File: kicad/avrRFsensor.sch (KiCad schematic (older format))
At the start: 26 parts, among them P1 CONN_1, P2 CONN_1, P3 CONN_1, P4 CONN_1, U1 ATMEGA168PA-A, U2 RFM69, X1 18MHz HC49USSMD

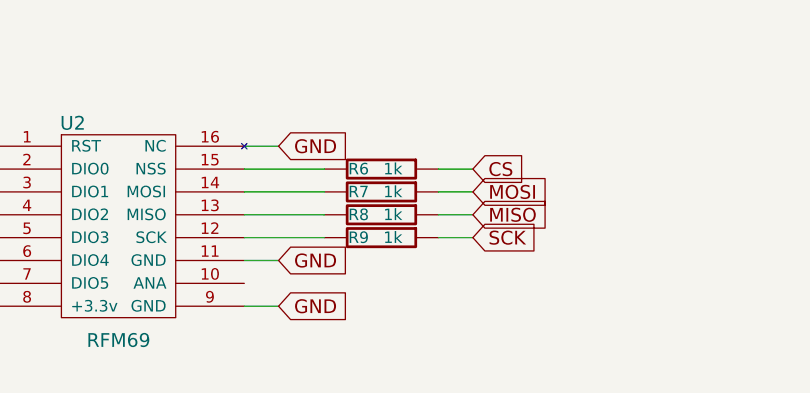
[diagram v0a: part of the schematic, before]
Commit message: fixed retransmit state for not save previous state and timer. Opposite retransmissions are forbidden. Kicad remade topology for low profile resonator and antenna and comparator pins.
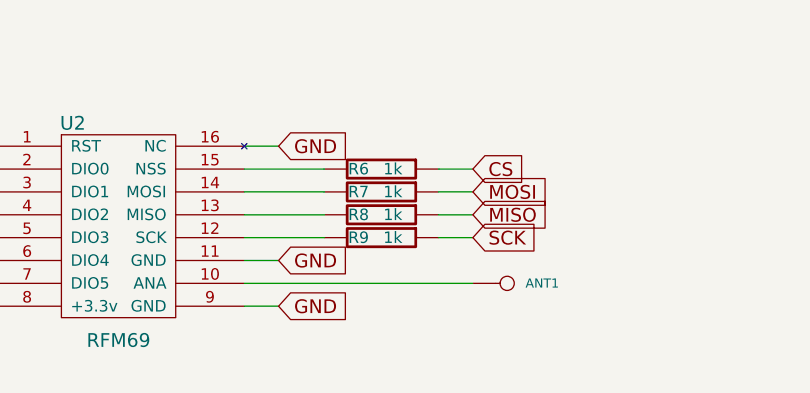
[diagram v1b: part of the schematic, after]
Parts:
- added ANT1: CONN_1, symbol CONN_1
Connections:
- net at U2.10 (ANA): now also ANT1.1
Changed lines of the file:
@@
 Sheet 1 1
 Title ""
-Date "10 may 2015"
+Date "11 may 2015"
 Rev ""
 Comp ""
@@
 $EndComp
 $Comp
-L GND #PWR2
+L GND #PWR01
 U 1 1 4E041C8A
 P 1000 6600
-F 0 "#PWR2" H 1000 6600 30  0001 C CNN
+F 0 "#PWR01" H 1000 6600 30  0001 C CNN
 F 1 "GND" H 1000 6530 30  0001 C CNN
 F 2 "" H 1000 6600 60  0001 C CNN
@@
 Connection ~ 1000 6050
 $Comp
-L VCC #PWR1
+L VCC #PWR02
 U 1 1 54B791F6
 P 1000 6000
-F 0 "#PWR1" H 1000 6100 30  0001 C CNN
+F 0 "#PWR02" H 1000 6100 30  0001 C CNN
 F 1 "VCC" H 1000 6100 30  0000 C CNN
 F 2 "" H 1000 6000 60  0000 C CNN
@@
 	9500 3700 9500 3950
 Connection ~ 9500 3950
+$Comp
+L CONN_1 ANT1
+U 1 1 55505F92
+P 5900 6250
+F 0 "ANT1" H 5980 6250 40  0000 L CNN
+F 1 "CONN_1" H 5900 6305 30  0001 C CNN
+F 2 "" H 5900 6250 60  0000 C CNN
+F 3 "" H 5900 6250 60  0000 C CNN
+	1    5900 6250
+	1    0    0    -1
+$EndComp
+Wire Wire Line
+	5750 6250 4750 6250
 $EndSCHEMATC
